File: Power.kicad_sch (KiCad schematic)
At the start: 33 parts, among them J31 DC Connector, U1 TPS62933, U2 TPS62933

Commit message: initial routing
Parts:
- added C41, C42: Cap 22uF, Capacitor_SMD:C_0805_2012Metric, symbol Kalid:Cap 22uF 0805
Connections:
- net +V5VUSB: now also C42.1
- net +V5VWALL: now also C41.1
- net GND: now also C41.2, C42.2

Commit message: finish routing
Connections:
- net 5VWALLSW: now reaches C10.2, L2.1, U2.5 (SW)
- net 5VUSBSW: now reaches C4.2, L1.1, U1.5 (SW)
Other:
- moved on the sheet: C10, C4
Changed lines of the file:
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@@
-	)
-	(junction
-		(at 176.53 88.9)
-		(diameter 0)
-		(color 0 0 0 0)
 	)
 	(junction
@@
 	)
 	(junction
+		(at 69.85 88.9)
+		(diameter 0)
+		(color 0 0 0 0)
+	)
+	(junction
 		(at 160.02 138.43)
 		(diameter 0)
@@
 	)
 	(junction
+		(at 177.8 88.9)
+		(diameter 0)
+		(color 0 0 0 0)
+	)
+	(junction
 		(at 207.01 88.9)
-		(diameter 0)
-		(color 0 0 0 0)
-	)
-	(junction
-		(at 68.58 88.9)
 		(diameter 0)
 		(color 0 0 0 0)
@@
 	(wire
 		(pts
-			(xy 176.53 88.9) (xy 179.07 88.9)
-		)
-		(stroke
-			(width 0)
-			(type default)
-		)
-	)
-	(wire
-		(pts
 			(xy 157.48 62.23) (xy 165.1 62.23)
 		)
@@
 	(wire
 		(pts
-			(xy 172.72 88.9) (xy 176.53 88.9)
+			(xy 172.72 88.9) (xy 177.8 88.9)
 		)
 		(stroke
@@
 	(wire
 		(pts
-			(xy 176.53 88.9) (xy 176.53 86.36)
-		)
-		(stroke
-			(width 0)
-			(type default)
-		)
-	)
-	(wire
-		(pts
-			(xy 64.77 88.9) (xy 68.58 88.9)
-		)
-		(stroke
-			(width 0)
-			(type default)
-		)
-	)
-	(wire
-		(pts
-			(xy 68.58 88.9) (xy 68.58 86.36)
+			(xy 177.8 88.9) (xy 177.8 86.36)
+		)
+		(stroke
+			(width 0)
+			(type default)
+		)
+	)
+	(wire
+		(pts
+			(xy 64.77 88.9) (xy 69.85 88.9)
+		)
+		(stroke
+			(width 0)
+			(type default)
+		)
+	)
+	(wire
+		(pts
+			(xy 69.85 88.9) (xy 69.85 86.36)
 		)
 		(stroke
@@
 	(wire
 		(pts
+			(xy 69.85 88.9) (xy 71.12 88.9)
+		)
+		(stroke
+			(width 0)
+			(type default)
+		)
+	)
+	(wire
+		(pts
 			(xy 146.05 138.43) (xy 146.05 140.97)
 		)
@@
 	(wire
 		(pts
-			(xy 172.72 81.28) (xy 176.53 81.28)
+			(xy 172.72 81.28) (xy 177.8 81.28)
 		)
 		(stroke
@@
 	(wire
 		(pts
+			(xy 177.8 88.9) (xy 179.07 88.9)
+		)
+		(stroke
+			(width 0)
+			(type default)
+		)
+	)
+	(wire
+		(pts
 			(xy 142.24 91.44) (xy 157.48 91.44)
 		)
@@
 	(wire
 		(pts
-			(xy 64.77 81.28) (xy 68.58 81.28)
+			(xy 64.77 81.28) (xy 69.85 81.28)
 		)
 		(stroke
@@
 	(wire
 		(pts
-			(xy 68.58 88.9) (xy 71.12 88.9)
-		)
-		(stroke
-			(width 0)
-			(type default)
-		)
-	)
-	(wire
-		(pts
 			(xy 107.95 151.13) (xy 116.84 151.13)
 		)
@@
 			(width 0)
 			(type default)
+		)
+	)
+	(label "5VUSBSW"
+		(at 69.85 88.9 180)
+		(effects
+			(font
+				(size 0.635 0.635)
+			)
+			(justify right bottom)
+		)
+	)
+	(label "5VWALLSW"
+		(at 177.8 88.9 180)
+		(effects
+			(font
+				(size 0.635 0.635)
+			)
+			(justify right bottom)
 		)
 	)
@@
 	(symbol
 		(lib_id "Kalid:Cap 100nF 0402")
-		(at 176.53 83.82 0)
+		(at 177.8 83.82 0)
 		(unit 1)
 		(exclude_from_sim no)
@@
 		(fields_autoplaced yes)
 		(property "Reference" "C10"
-			(at 179.07 82.5499 0)
+			(at 180.34 82.5499 0)
 			(effects
 				(font
@@
 		)
 		(property "Value" "Cap 100nF"
-			(at 176.784 85.852 0)
+			(at 178.054 85.852 0)
 			(effects
 				(font
@@
 		)
 		(property "Footprint" "Capacitor_SMD:C_0402_1005Metric"
-			(at 176.53 96.52 0)
+			(at 177.8 96.52 0)
 			(effects
 				(font
@@
 		)
 		(property "Datasheet" "https://www.lcsc.com/datasheet/lcsc_datasheet_1811081532_Murata-Electronics-GRM033R61A104KE15D_C76934.pdf"
-			(at 176.53 91.44 0)
+			(at 177.8 91.44 0)
 			(effects
 				(font
@@
 		)
 		(property "Description" "50V 100nF X7R ±10% 0402 Multilayer Ceramic Capacitors MLCC - SMD/SMT ROHS"
-			(at 176.53 83.82 0)
+			(at 177.8 83.82 0)
 			(effects
 				(font
@@
 		)
 		(property "Val" "100nF"
-			(at 179.07 85.0899 0)
+			(at 180.34 85.0899 0)
 			(effects
 				(font
@@
 		)
 		(property "Manufacturer" "Samsung Electro-Mechanics"
-			(at 176.53 93.98 0)
+			(at 177.8 93.98 0)
 			(effects
 				(font
@@
 		)
 		(property "MPN" "CL05B104KB54PNC"
-			(at 176.53 88.9 0)
+			(at 177.8 88.9 0)
 			(effects
 				(font
@@
 		)
 		(property "LCSC" "C307331"
-			(at 176.53 83.82 90)
+			(at 177.8 83.82 90)
 			(effects
 				(font
@@
 	(symbol
 		(lib_id "Kalid:Cap 100nF 0402")
-		(at 68.58 83.82 0)
+		(at 69.85 83.82 0)
 		(unit 1)
 		(exclude_from_sim no)
@@
 		(fields_autoplaced yes)
 		(property "Reference" "C4"
-			(at 71.12 82.5499 0)
+			(at 72.39 82.5499 0)
 			(effects
 				(font
@@
 		)
 		(property "Value" "Cap 100nF"
-			(at 68.834 85.852 0)
+			(at 70.104 85.852 0)
 			(effects
 				(font
@@
 		)
 		(property "Footprint" "Capacitor_SMD:C_0402_1005Metric"
-			(at 68.58 96.52 0)
+			(at 69.85 96.52 0)
 			(effects
 				(font
@@
 		)
 		(property "Datasheet" "https://www.lcsc.com/datasheet/lcsc_datasheet_1811081532_Murata-Electronics-GRM033R61A104KE15D_C76934.pdf"
-			(at 68.58 91.44 0)
+			(at 69.85 91.44 0)
 			(effects
 				(font
@@
 		)
 		(property "Description" "50V 100nF X7R ±10% 0402 Multilayer Ceramic Capacitors MLCC - SMD/SMT ROHS"
-			(at 68.58 83.82 0)
+			(at 69.85 83.82 0)
 			(effects
 				(font
@@
 		)
 		(property "Val" "100nF"
-			(at 71.12 85.0899 0)
+			(at 72.39 85.0899 0)
 			(effects
 				(font
@@
 		)
 		(property "Manufacturer" "Samsung Electro-Mechanics"
-			(at 68.58 93.98 0)
+			(at 69.85 93.98 0)
 			(effects
 				(font
@@
 		)
 		(property "MPN" "CL05B104KB54PNC"
-			(at 68.58 88.9 0)
+			(at 69.85 88.9 0)
 			(effects
 				(font
@@
 		)
 		(property "LCSC" "C307331"
-			(at 68.58 83.82 90)
-			(effects
-				(font
+			(at 69.85 83.82 90)
+			(effects
+				(font

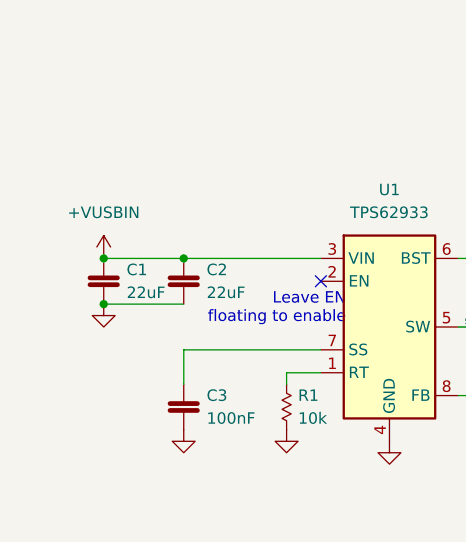
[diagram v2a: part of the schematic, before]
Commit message: add testpoint
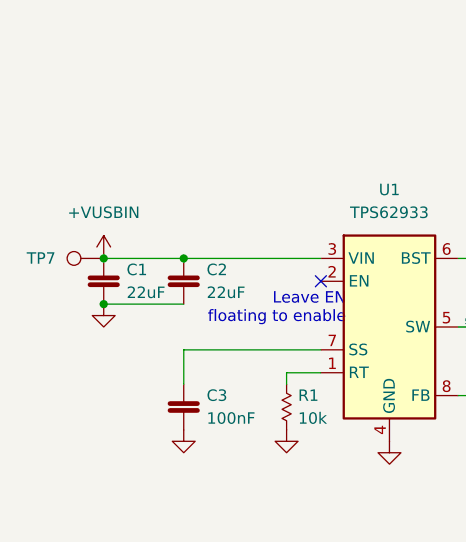
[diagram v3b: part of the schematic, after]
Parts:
- added TP7: TestPoint, TestPoint:TestPoint_Pad_D1.5mm, symbol Connector:TestPoint
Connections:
- net +VUSBIN: now also TP7.1
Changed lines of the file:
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@@
+	)
+	(symbol
+		(lib_id "Connector:TestPoint")
+		(at 25.4 81.28 90)
+		(mirror x)
+		(unit 1)
+		(exclude_from_sim no)
+		(in_bom yes)
+		(on_board yes)
+		(dnp no)
+		(property "Reference" "TP7"
+			(at 20.066 81.28 90)
+			(effects
+				(font
+					(size 1.27 1.27)
+				)
+				(justify left)
+			)
+		)
+		(property "Value" "TestPoint"
+			(at 20.32 82.5499 90)
+			(effects
+				(font
+					(size 1.27 1.27)
+				)
+				(justify left)
+				(hide yes)
+			)
+		)
+		(property "Footprint" "TestPoint:TestPoint_Pad_D1.5mm"
+			(at 25.4 86.36 0)
+			(effects
+				(font
+					(size 1.27 1.27)
+				)
+				(hide yes)
+			)
+		)
+		(property "Datasheet" "~"
+			(at 25.4 86.36 0)
+			(effects
+				(font
+					(size 1.27 1.27)
+				)
+				(hide yes)
+			)
+		)
+		(property "Description" "test point"
+			(at 25.4 81.28 0)
+			(effects
+				(font
+					(size 1.27 1.27)
+				)
+				(hide yes)
+			)
+		)
+		(pin "1"
+		)
+		(instances
+			(project "Kalid"
+				(path "/5c5b6a50-9d49-4bf7-888b-87984473892a/785a3ac2-5e82-4fd1-812e-debec2fc492c/61f87398-b322-411d-869c-748c609586ba"
+					(reference "TP7")
+					(unit 1)
+				)
+			)
+		)
 	)
 	(symbol

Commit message: develop evt2
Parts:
- added R50, R51, R52, R53, R54, R55, R56, R57: R 10k 0402, Resistor_SMD:R_0402_1005Metric, symbol Kalid:R 10k 0402
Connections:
- net at R3.2, U1.8 (FB): now also R52.1; no longer R2.1
- net at R4.1, R5.1: now also R53.1; no longer R2.2
- net at R10.1, R7.1: now also R54.1; no longer R8.2
- new net: R51.1, R53.2
- new net: R2.2, R51.2
- new net: R55.1, R8.2
- new net: R55.2, R57.1
- new net: R2.1, R50.2
- new net: R54.2, R56.1
- new net: R56.2, R57.2
- new net: R50.1, R52.2
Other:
- moved on the sheet: R3, R9

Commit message: tag schematic and pcb as evt2
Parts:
- C1, C11, C12, C13, C14, C2, C41, C42, C5, C6, C7, C8: LCSC C602037 -> C45783
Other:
- title: (none) -> Kalid
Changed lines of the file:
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@@
 	(generator_version "9.0")
 	(paper "A4")
+	(title_block
+		(title "Kalid")
+		(date "2025-08-18")
+		(rev "EVT2")
+	)
 	(rectangle
 		(start 85.09 106.68)
@@
 			)
 		)
-		(property "LCSC" "C602037"
+		(property "LCSC" "C45783"
 			(at 149.86 140.97 90)
 			(effects
@@
 			)
 		)
-		(property "LCSC" "C602037"
+		(property "LCSC" "C45783"
 			(at 25.4 83.82 90)
 			(effects
@@
 			)
 		)
-		(property "LCSC" "C602037"
+		(property "LCSC" "C45783"
 			(at 116.84 140.97 90)
 			(effects
@@
 			)
 		)
-		(property "LCSC" "C602037"
+		(property "LCSC" "C45783"
 			(at 116.84 153.67 90)
 			(effects
@@
 			)
 		)
-		(property "LCSC" "C602037"
+		(property "LCSC" "C45783"
 			(at 160.02 140.97 90)
 			(effects
@@
 			)
 		)
-		(property "LCSC" "C602037"
+		(property "LCSC" "C45783"
 			(at 133.35 83.82 90)
 			(effects
@@
 			)
 		)
-		(property "LCSC" "C602037"
+		(property "LCSC" "C45783"
 			(at 217.17 91.44 90)
 			(effects
@@
 			)
 		)
-		(property "LCSC" "C602037"
+		(property "LCSC" "C45783"
 			(at 109.22 91.44 90)
 			(effects
@@
 			)
 		)
-		(property "LCSC" "C602037"
+		(property "LCSC" "C45783"
 			(at 34.29 83.82 90)
 			(effects
@@
 			)
 		)
-		(property "LCSC" "C602037"
+		(property "LCSC" "C45783"
 			(at 99.06 91.44 90)
 			(effects
@@
 			)
 		)
-		(property "LCSC" "C602037"
+		(property "LCSC" "C45783"
 			(at 207.01 91.44 90)
 			(effects
@@
 			)
 		)
-		(property "LCSC" "C602037"
+		(property "LCSC" "C45783"
 			(at 142.24 83.82 90)
 			(effects

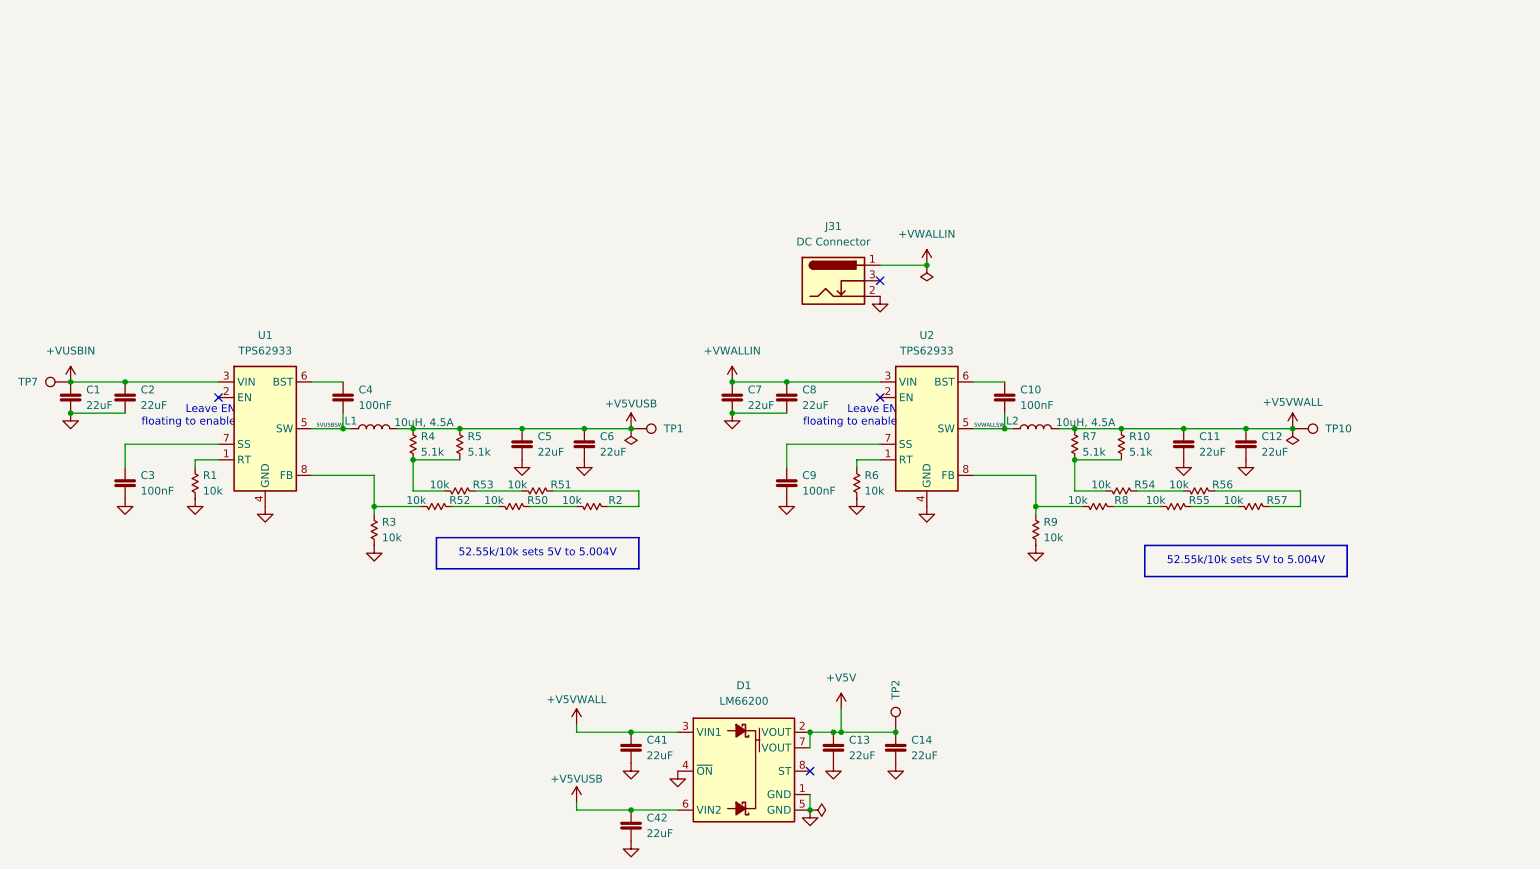
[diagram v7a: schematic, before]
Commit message: add second power circuit
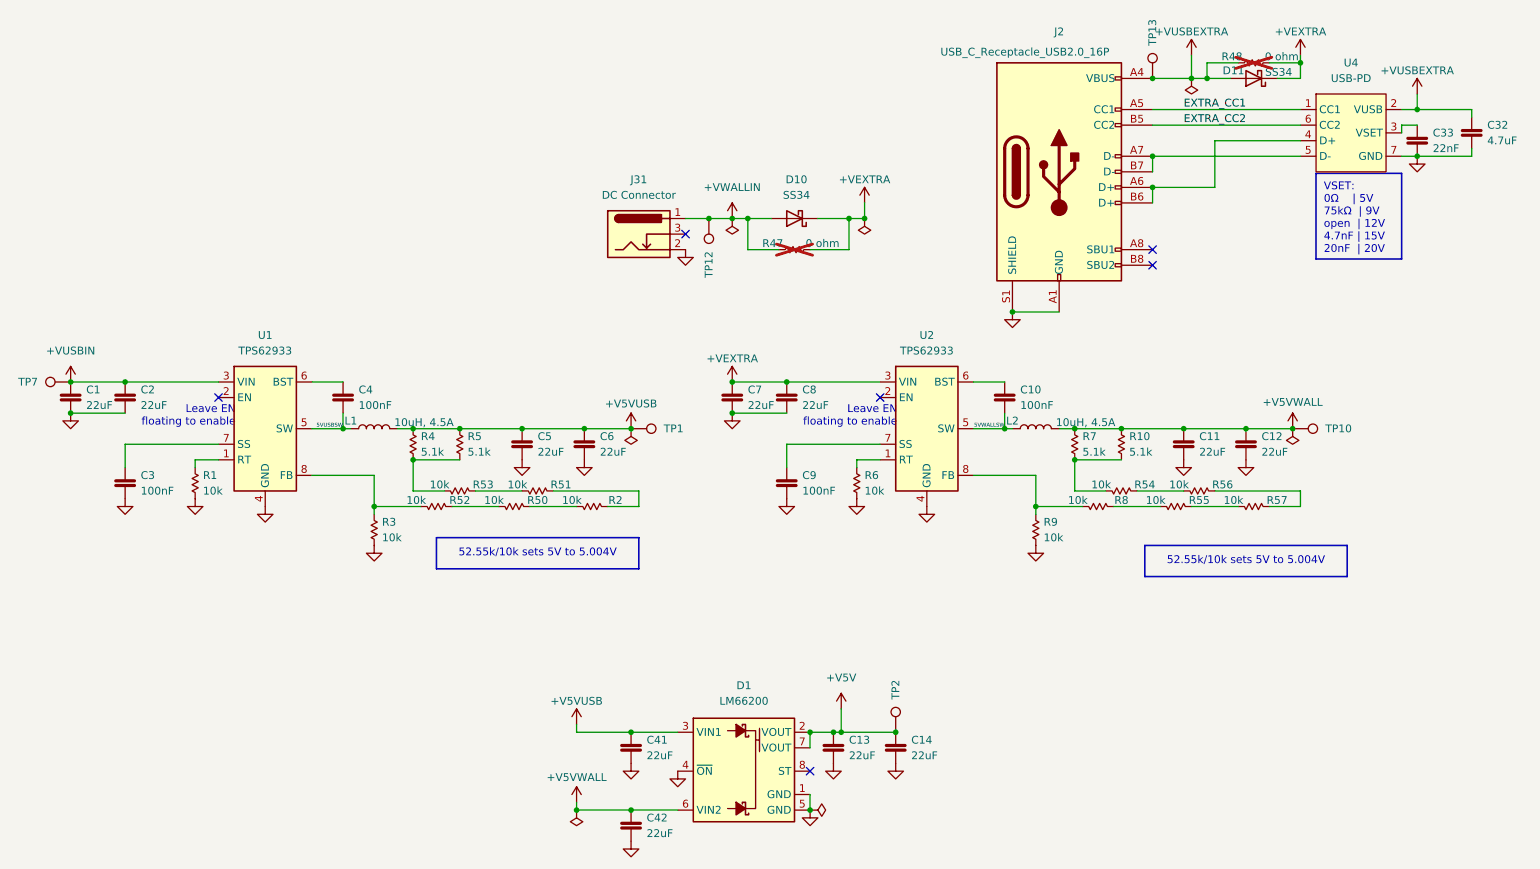
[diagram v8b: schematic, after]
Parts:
- added C32: Cap 4.7uF 0402, Capacitor_SMD:C_0402_1005Metric, symbol Kalid:Cap 4.7uF 0402
- added C33: Cap 22nF 0402, Capacitor_SMD:C_0402_1005Metric, symbol Kalid:Cap 22nF 0402
- added D10, D11: SS34, Diode_SMD:D_SMA, symbol Diode:SS34
- added J2: USB_C_Receptacle_USB2.0_16P, Kalid:USB_C_Receptacle_HRO_TYPE-C-31-M-12, symbol Connector:USB_C_Receptacle_USB2.0_16P
- added R47, R48: R 0 ohm 0402, Resistor_SMD:R_0402_1005Metric, symbol Kalid:R 0 ohm 0402
- added TP12, TP13: TestPoint, TestPoint:TestPoint_Pad_D1.5mm, symbol Connector:TestPoint
- added U4: USB-PD, Package_DFN_QFN:DFN-6-1EP_2x2mm_P0.65mm_EP1x1.6mm, symbol Kalid:HUSB237-AA001-DN06R
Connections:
- net +V5VUSB: now also C41.1, D1.3 (VIN1); no longer C42.1, D1.6 (VIN2)
- net +V5VWALL: now also C42.1, D1.6 (VIN2); no longer C41.1, D1.3 (VIN1)
- net +VWALLIN: now also D10.2 (A), R47.2, TP12.1; no longer C7.1, C8.1, U2.3 (VIN)
- net GND: now also C32.2, C33.2, J2.A1 (GND), J2.A12 (GND), J2.B1 (GND), J2.B12 (GND), J2.S1 (SHIELD), U4.7 (GND)
- new net: C33.1, U4.3 (VSET)
- new net: J2.A6 (D+), J2.B6 (D+), U4.4 (D+)
- new net: J2.A7 (D-), J2.B7 (D-), U4.5 (D-)
- new net +VEXTRA: C7.1, C8.1, D10.1 (K), D11.1 (K), R47.1, R48.1, U2.3 (VIN)
- new net +VUSBEXTRA: C32.1, D11.2 (A), J2.A4 (VBUS), J2.A9 (VBUS), J2.B4 (VBUS), J2.B9 (VBUS), R48.2, TP13.1, U4.2 (VUSB)
- new net EXTRA_CC1: J2.A5 (CC1), U4.1 (CC1)
- new net EXTRA_CC2: J2.B5 (CC2), U4.6 (CC2)
- no-connect marks 4 -> 6
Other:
- note added: "VSET: 0Ω | 5V 75kΩ | 9V open | 12V 4.7nF | 15V 20nF | 20V"
- moved on the sheet: J31
